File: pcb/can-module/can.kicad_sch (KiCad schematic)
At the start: 17 parts, among them U2 MCP25625x-x-ML, U4 MCP25625x-x-ML, X2 X322516MOB4SI

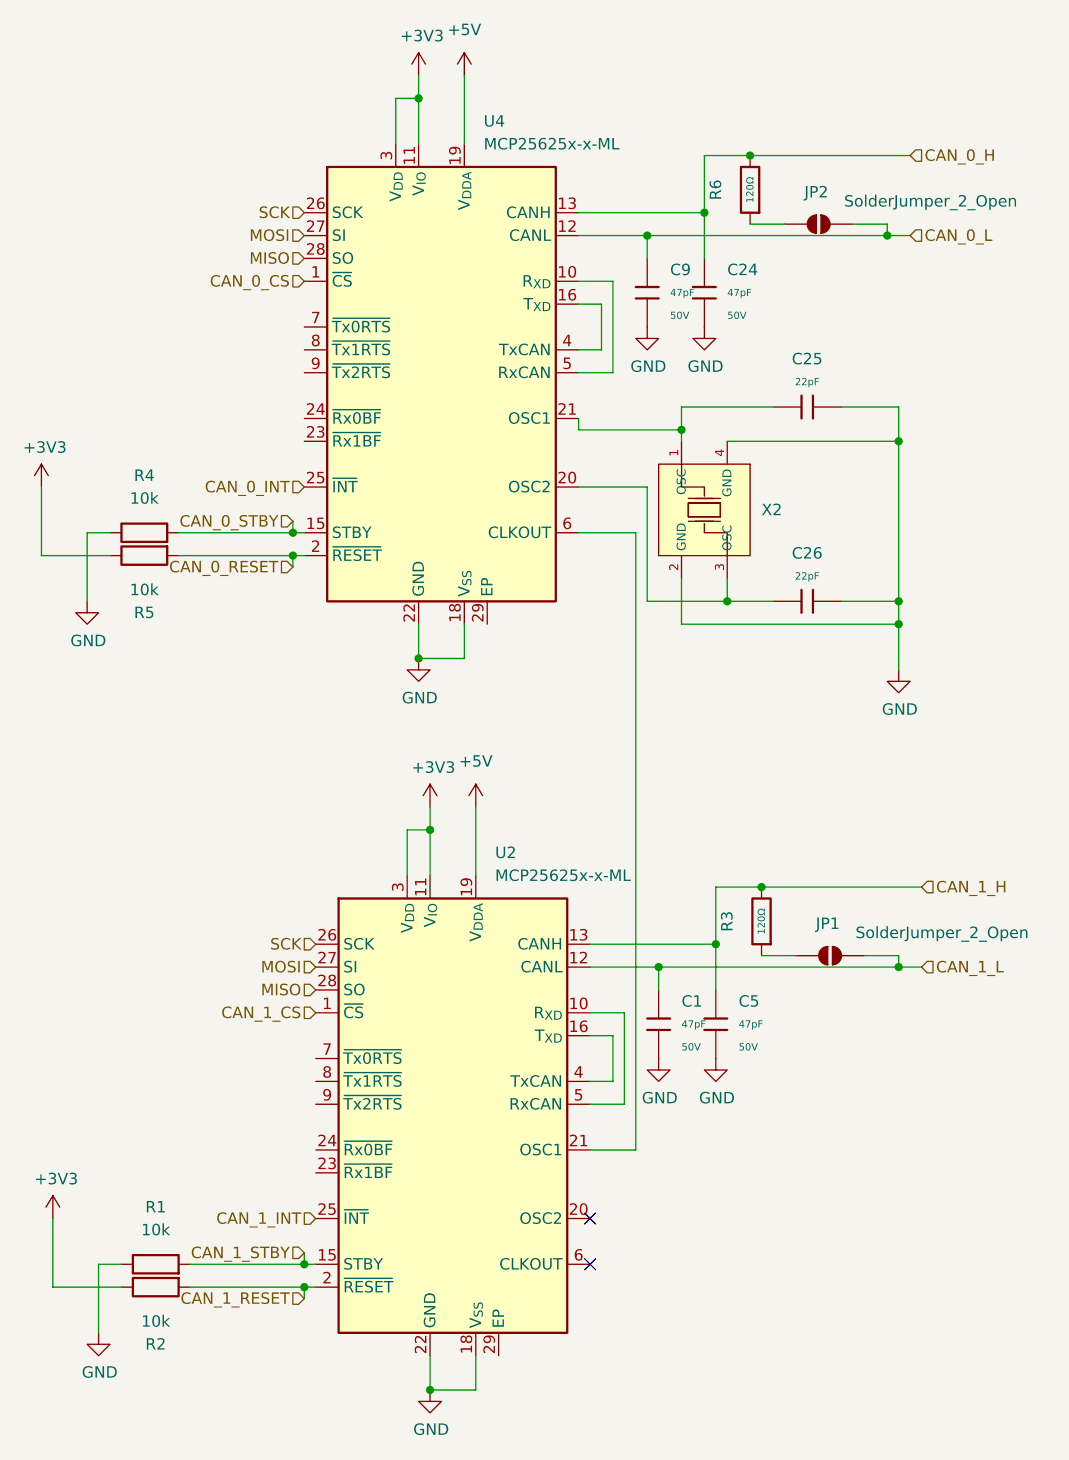
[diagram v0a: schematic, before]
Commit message: Fix ERC errors
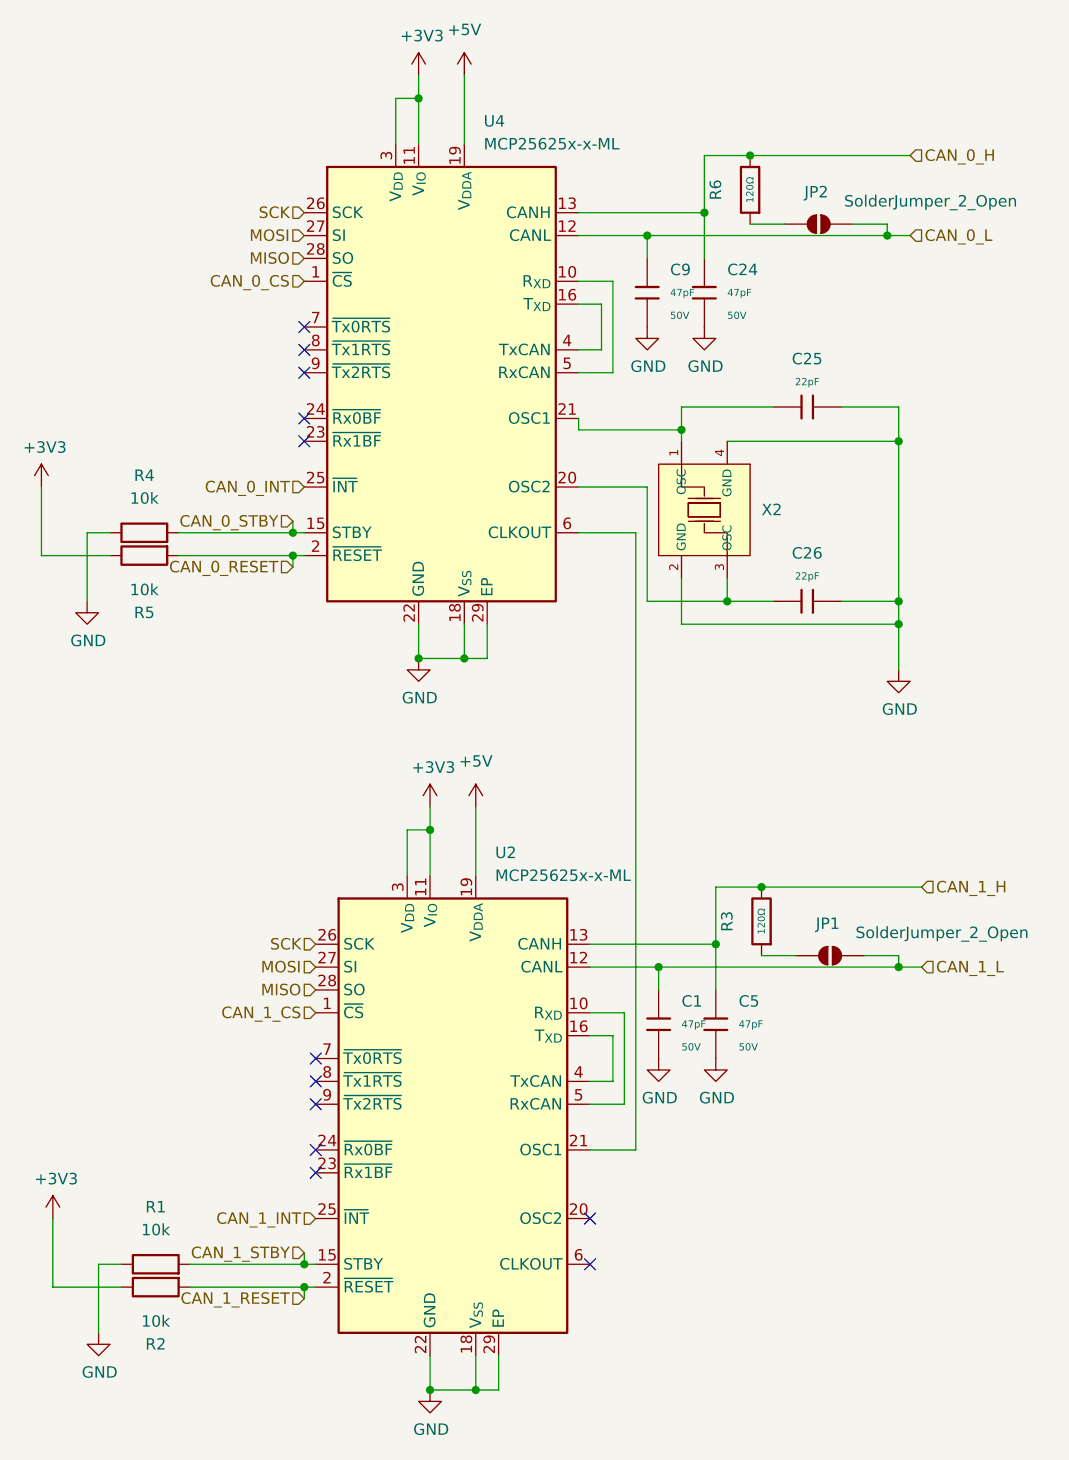
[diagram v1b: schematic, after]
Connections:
- net GND: now also U2.29 (EP), U4.29 (EP)
- no-connect marks 2 -> 12
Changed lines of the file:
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@@
 	(paper "A4")
 	(junction
+		(at 110.49 166.37)
+		(diameter 0)
+		(color 0 0 0 0)
+	)
+	(junction
 		(at 104.14 22.86)
 		(diameter 0)
@@
 	)
 	(junction
+		(at 109.22 85.09)
+		(diameter 0)
+		(color 0 0 0 0)
+	)
+	(junction
 		(at 157.48 60.96)
 		(diameter 0)
@@
 	)
 	(no_connect
+		(at 91.44 60.96)
+	)
+	(no_connect
+		(at 92.71 142.24)
+	)
+	(no_connect
+		(at 92.71 134.62)
+	)
+	(no_connect
+		(at 91.44 50.8)
+	)
+	(no_connect
+		(at 92.71 139.7)
+	)
+	(no_connect
+		(at 92.71 129.54)
+	)
+	(no_connect
+		(at 92.71 132.08)
+	)
+	(no_connect
+		(at 91.44 58.42)
+	)
+	(no_connect
+		(at 91.44 48.26)
+	)
+	(no_connect
+		(at 91.44 53.34)
+	)
+	(no_connect
 		(at 123.19 152.4)
 	)
@@
 	(wire
 		(pts
+			(xy 113.03 166.37) (xy 113.03 162.56)
+		)
+		(stroke
+			(width 0)
+			(type default)
+		)
+	)
+	(wire
+		(pts
 			(xy 133.35 57.15) (xy 143.51 57.15)
 		)
@@
 	(wire
 		(pts
+			(xy 111.76 85.09) (xy 111.76 81.28)
+		)
+		(stroke
+			(width 0)
+			(type default)
+		)
+	)
+	(wire
+		(pts
 			(xy 77.47 73.66) (xy 90.17 73.66)
 		)
@@
 	(wire
 		(pts
+			(xy 109.22 85.09) (xy 111.76 85.09)
+		)
+		(stroke
+			(width 0)
+			(type default)
+		)
+	)
+	(wire
+		(pts
 			(xy 135.89 29.21) (xy 140.97 29.21)
 		)
@@
 		)
 		(stroke
+			(width 0)
+			(type default)
+		)
+	)
+	(wire
+		(pts
+			(xy 110.49 166.37) (xy 113.03 166.37)
+		)
+		(stroke

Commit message: Board layout
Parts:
- renumbered C5 to C3, C1 to C4, C24 to C5, C9 to C6, C26 to C7, C25 to C8, R3 to R1, R6 to R2, R4 to R3, R1 to R6, R2 to R7, R5 to R9, JP1 to TERM_RES_1, JP2 to TERM_RES_2, U4 to U3, X2 to X1
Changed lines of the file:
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@@
 		(on_board yes)
 		(dnp no)
-		(property "Reference" "C26"
+		(property "Reference" "C7"
 			(at 147.32 73.406 90)
 			(effects
@@
 			(project "can-module"
 				(path "/8c0b3d8b-46d3-4173-ab1e-a61765f77d61/43274a1c-f068-4227-8d4c-f55bb0b2e49a"
-					(reference "C26")
+					(reference "C7")
 					(unit 1)
 				)
@@
 		(dnp no)
 		(fields_autoplaced yes)
-		(property "Reference" "R1"
+		(property "Reference" "R6"
 			(at 74.93 146.05 90)
 			(effects
@@
 			(project "can-module"
 				(path "/8c0b3d8b-46d3-4173-ab1e-a61765f77d61/43274a1c-f068-4227-8d4c-f55bb0b2e49a"
-					(reference "R1")
+					(reference "R6")
 					(unit 1)
 				)
@@
 		(dnp no)
 		(fields_autoplaced yes)
-		(property "Reference" "R4"
+		(property "Reference" "R3"
 			(at 73.66 64.77 90)
 			(effects
@@
 			(project "can-module"
 				(path "/8c0b3d8b-46d3-4173-ab1e-a61765f77d61/43274a1c-f068-4227-8d4c-f55bb0b2e49a"
-					(reference "R4")
+					(reference "R3")
 					(unit 1)
 				)
@@
 		(on_board yes)
 		(dnp no)
-		(property "Reference" "JP1"
+		(property "Reference" "TERM_RES_1"
 			(at 149.606 114.554 0)
 			(effects
@@
 			(project "can-module"
 				(path "/8c0b3d8b-46d3-4173-ab1e-a61765f77d61/43274a1c-f068-4227-8d4c-f55bb0b2e49a"
-					(reference "JP1")
+					(reference "TERM_RES_1")
 					(unit 1)
 				)
@@
 		(on_board yes)
 		(dnp no)
-		(property "Reference" "JP2"
+		(property "Reference" "TERM_RES_2"
 			(at 148.336 33.274 0)
 			(effects
@@
 			(project "can-module"
 				(path "/8c0b3d8b-46d3-4173-ab1e-a61765f77d61/43274a1c-f068-4227-8d4c-f55bb0b2e49a"
-					(reference "JP2")
+					(reference "TERM_RES_2")
 					(unit 1)
 				)
@@
 		(dnp no)
 		(fields_autoplaced yes)
-		(property "Reference" "C1"
+		(property "Reference" "C4"
 			(at 133.35 123.1899 0)
 			(effects
@@
 			(project "can-module"
 				(path "/8c0b3d8b-46d3-4173-ab1e-a61765f77d61/43274a1c-f068-4227-8d4c-f55bb0b2e49a"
-					(reference "C1")
+					(reference "C4")
 					(unit 1)
 				)
@@
 		(on_board yes)
 		(dnp no)
-		(property "Reference" "C25"
+		(property "Reference" "C8"
 			(at 147.32 51.816 90)
 			(effects
@@
 			(project "can-module"
 				(path "/8c0b3d8b-46d3-4173-ab1e-a61765f77d61/43274a1c-f068-4227-8d4c-f55bb0b2e49a"
-					(reference "C25")
+					(reference "C8")
 					(unit 1)
 				)
@@
 		(on_board yes)
 		(dnp no)
-		(property "Reference" "R6"
+		(property "Reference" "R2"
 			(at 137.16 33.02 90)
 			(effects
@@
 			(project "can-module"
 				(path "/8c0b3d8b-46d3-4173-ab1e-a61765f77d61/43274a1c-f068-4227-8d4c-f55bb0b2e49a"
-					(reference "R6")
+					(reference "R2")
 					(unit 1)
 				)
@@
 		(dnp no)
 		(fields_autoplaced yes)
-		(property "Reference" "U4"
+		(property "Reference" "U3"
 			(at 111.3633 25.4 0)
 			(effects
@@
 			(project "can-module"
 				(path "/8c0b3d8b-46d3-4173-ab1e-a61765f77d61/43274a1c-f068-4227-8d4c-f55bb0b2e49a"
-					(reference "U4")
+					(reference "U3")
 					(unit 1)
 				)
@@
 		(dnp no)
 		(fields_autoplaced yes)
-		(property "Reference" "C24"
+		(property "Reference" "C5"
 			(at 138.43 41.9099 0)
 			(effects
@@
 			(project "can-module"
 				(path "/8c0b3d8b-46d3-4173-ab1e-a61765f77d61/43274a1c-f068-4227-8d4c-f55bb0b2e49a"
-					(reference "C24")
+					(reference "C5")
 					(unit 1)
 				)
@@
 		(on_board yes)
 		(dnp no)
-		(property "Reference" "R2"
+		(property "Reference" "R7"
 			(at 74.93 161.29 90)
 			(effects
@@
 			(project "can-module"
 				(path "/8c0b3d8b-46d3-4173-ab1e-a61765f77d61/43274a1c-f068-4227-8d4c-f55bb0b2e49a"
-					(reference "R2")
+					(reference "R7")
 					(unit 1)
 				)
@@
 		(dnp no)
 		(fields_autoplaced yes)
-		(property "Reference" "X2"
+		(property "Reference" "X1"
 			(at 142.24 68.5799 90)
 			(effects
@@
 			(project "can-module"
 				(path "/8c0b3d8b-46d3-4173-ab1e-a61765f77d61/43274a1c-f068-4227-8d4c-f55bb0b2e49a"
-					(reference "X2")
+					(reference "X1")
 					(unit 1)
 				)
@@
 		(dnp no)
 		(fields_autoplaced yes)
-		(property "Reference" "C5"
+		(property "Reference" "C3"
 			(at 139.7 123.1899 0)
 			(effects
@@
 			(project "can-module"
 				(path "/8c0b3d8b-46d3-4173-ab1e-a61765f77d61/43274a1c-f068-4227-8d4c-f55bb0b2e49a"
-					(reference "C5")
+					(reference "C3")
 					(unit 1)
 				)
@@
 		(dnp no)
 		(fields_autoplaced yes)
-		(property "Reference" "C9"
+		(property "Reference" "C6"
 			(at 132.08 41.9099 0)
 			(effects
@@
 			(project "can-module"
 				(path "/8c0b3d8b-46d3-4173-ab1e-a61765f77d61/43274a1c-f068-4227-8d4c-f55bb0b2e49a"
-					(reference "C9")
+					(reference "C6")
 					(unit 1)
 				)
@@
 		(on_board yes)
 		(dnp no)
-		(property "Reference" "R5"
+		(property "Reference" "R9"
 			(at 73.66 80.01 90)
 			(effects
@@
 			(project "can-module"
 				(path "/8c0b3d8b-46d3-4173-ab1e-a61765f77d61/43274a1c-f068-4227-8d4c-f55bb0b2e49a"
-					(reference "R5")
+					(reference "R9")
 					(unit 1)
 				)
@@
 		(on_board yes)
 		(dnp no)
-		(property "Reference" "R3"
+		(property "Reference" "R1"
 			(at 138.43 114.3 90)
 			(effects
@@
 			(project "can-module"
 				(path "/8c0b3d8b-46d3-4173-ab1e-a61765f77d61/43274a1c-f068-4227-8d4c-f55bb0b2e49a"
-					(reference "R3")
+					(reference "R1")
 					(unit 1)
 				)
